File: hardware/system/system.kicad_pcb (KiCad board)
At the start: 2 copper layers, 226.6 x 87.2 mm, 45 parts, among them J1 CART_SOCKET_28P, J2 EXT_PINS, SW1 POWER, SW2 RESET, SW3 A, SW4 B, SW5 UP, SW6 DN, SW7 LF, SW8 RT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

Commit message: Bump system to 1.0-dev1
- Mirror charge symbol on back shell
- Remove button 3D models
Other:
- board text added: "V1.0-dev1"
- board text removed: "V1.0-dev0"

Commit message: Rewire screen regulator Vin to RAW
- Also add schematic PDFs
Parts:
- removed the BZ1 at (93.5, 140.2)
- removed the U3 at (63.3, 95.0)
- added REF**: Buzzer, system:BUZZER_CUTOUT, F.Cu at (93.5, 140.2)
- added REF**: SPI_DISPLAY, system:DIYMORE_2.42_IN_OLED_CUTOUT, F.Cu at (63.3, 95.0)
- D1, D2: value SB1100 -> SB120
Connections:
- C1 pad 1: VCC -> Net-(C1-Pad1)
- J1 pad 26: Net-(J1-Pad26) -> Net-(C1-Pad1)
- SW1 pad 3: Net-(J1-Pad26) -> Net-(C1-Pad1)
- U2 pad 2: VCC -> Net-(C1-Pad1)
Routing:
- net Net-(C1-Pad1): track 0.00 -> 150.4 mm
- net Net-(J1-Pad26): track 54.5 -> 0.00 mm
- net VCC: track 110.1 -> 78.5 mm
- net GND: vias 9 -> 10
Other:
- board text added: "V1.0-dev2"
- board text removed: "V1.0-dev1"

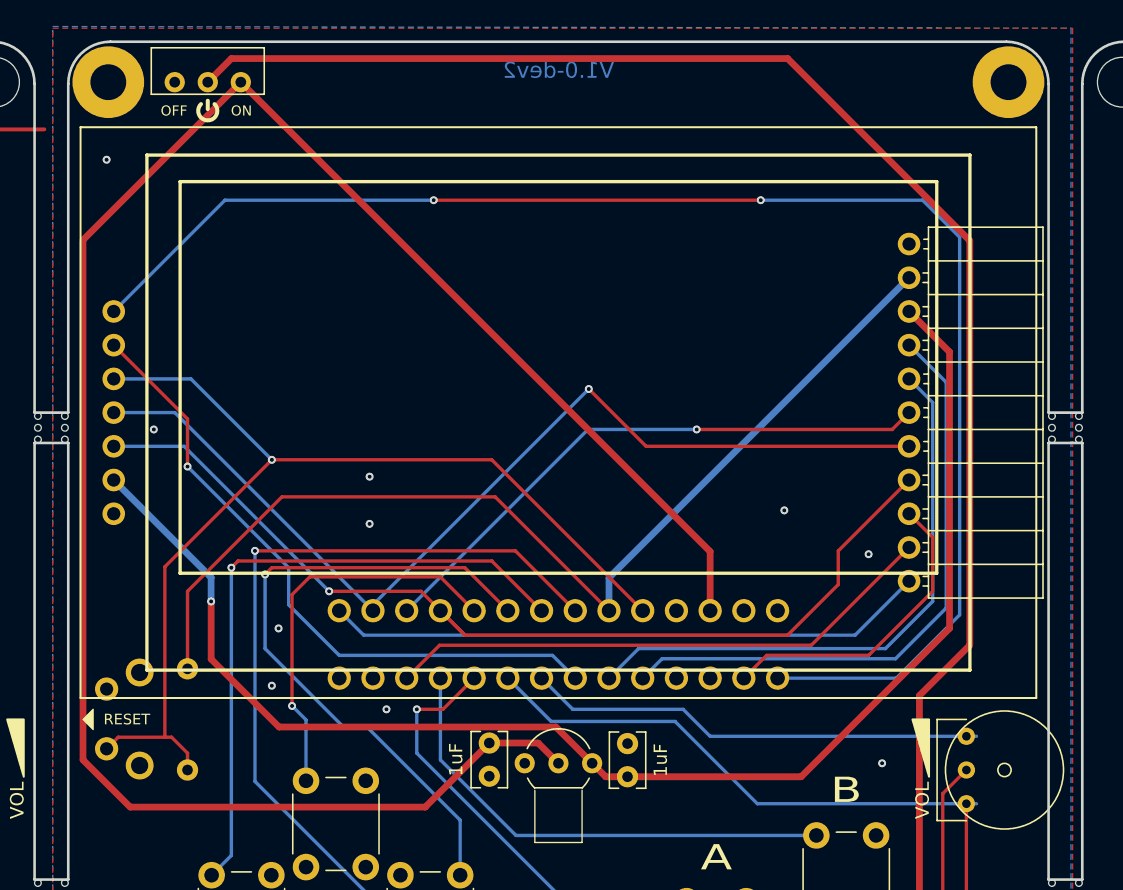
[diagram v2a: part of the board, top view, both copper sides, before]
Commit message: Connect power to VCC instead of RAW
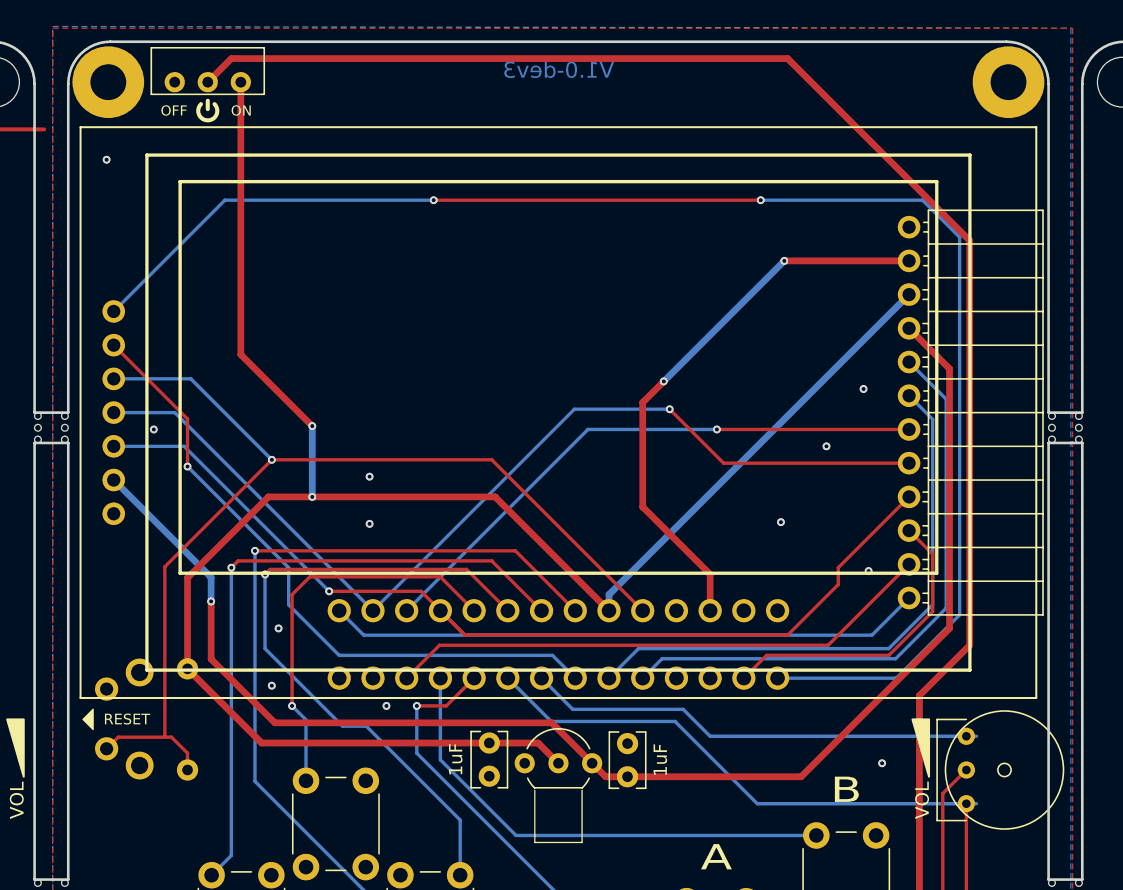
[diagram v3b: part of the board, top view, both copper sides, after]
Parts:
- removed the REF** at (93.5, 140.2)
- removed the REF** at (63.3, 95.0)
- removed the RV1 at (99.4, 121.9)
- added ?: SPI_DISPLAY, system:DIYMORE_2.42_IN_OLED_CUTOUT, F.Cu at (63.3, 95.0)
- added ?: Buzzer, system:BUZZER_CUTOUT, F.Cu at (93.5, 140.2)
- added ?: VOLUME 10K, system:VOLUME_LABEL, F.Cu at (99.4, 121.9)
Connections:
- C1 pad 1: Net-(C1-Pad1) -> VCC
- J1 pad 26: Net-(C1-Pad1) -> RAW
- J2 pad 10: D9_A9 -> D0
- J2 pad 11: D10_A10 -> D9_A9
- J2 pad 2: VCC -> RAW
- J2 pad 3: 3V3 -> VCC
- J2 pad 4: SDA -> 3V3
- J2 pad 5: SCL -> SDA
- J2 pad 6: MISO -> SCL
- J2 pad 7: MOSI -> MISO
- J2 pad 8: SCK -> MOSI
- J2 pad 9: D0 -> SCK
- SW1 pad 3: Net-(C1-Pad1) -> VCC
- U2 pad 2: Net-(C1-Pad1) -> VCC
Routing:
- net Net-(C1-Pad1): track 150.4 -> 0.00 mm
- net VCC: track 78.5 -> 142.2 mm, vias 0 -> 2
- net RAW: track 0.00 -> 42.3 mm, vias 0 -> 2
- net SDA: track 46.0 -> 44.7 mm
- net SCK: track 74.7 -> 73.5 mm
- net 3V3: track 105.6 -> 104.3 mm
- net SCL: track 44.3 -> 43.2 mm
- net MOSI: track 75.1 -> 74.1 mm
- net D9_A9: track 41.9 -> 41.4 mm
- net D10_A10: track 45.4 -> 44.8 mm
- net MISO: track 44.0 -> 43.5 mm
- net GND: vias 10 -> 12
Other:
- board text added: "V1.0-dev3"
- board text removed: "V1.0-dev2"

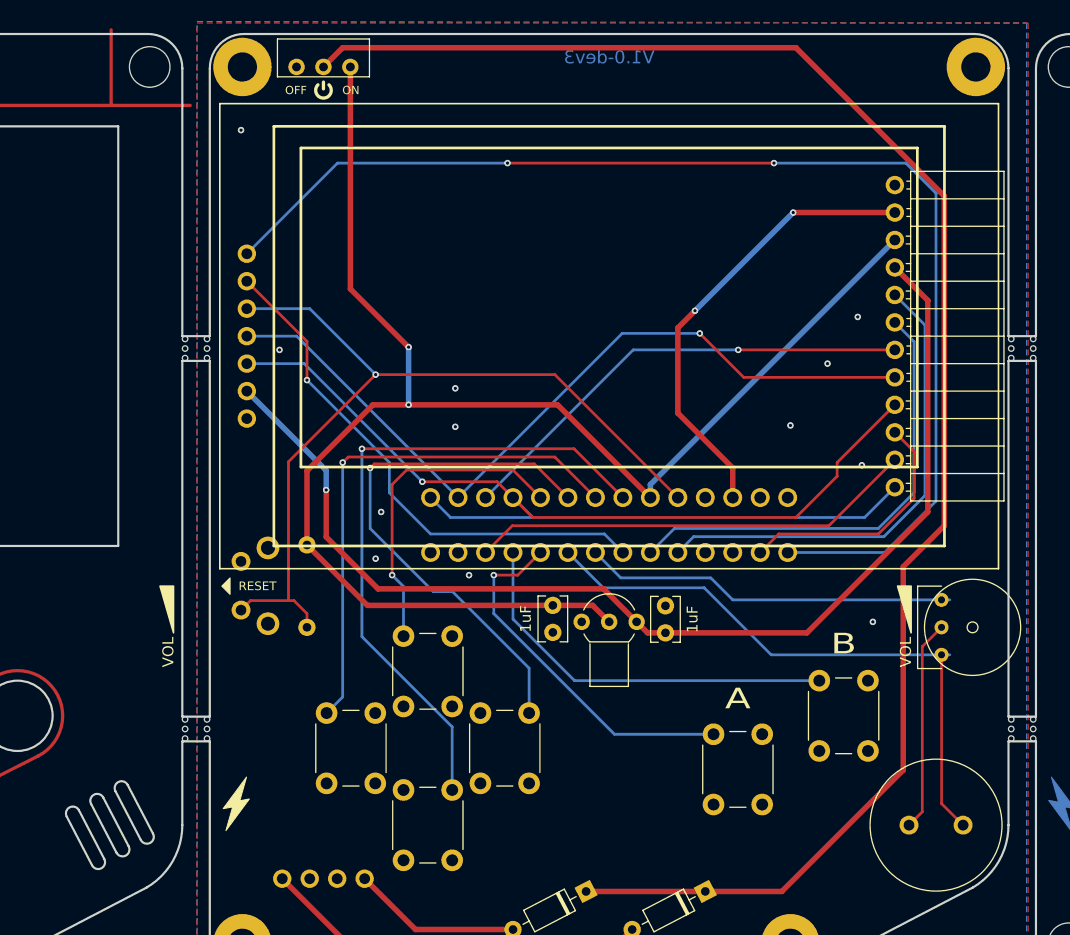
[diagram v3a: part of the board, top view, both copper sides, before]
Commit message: Connect display RES to D0/RX
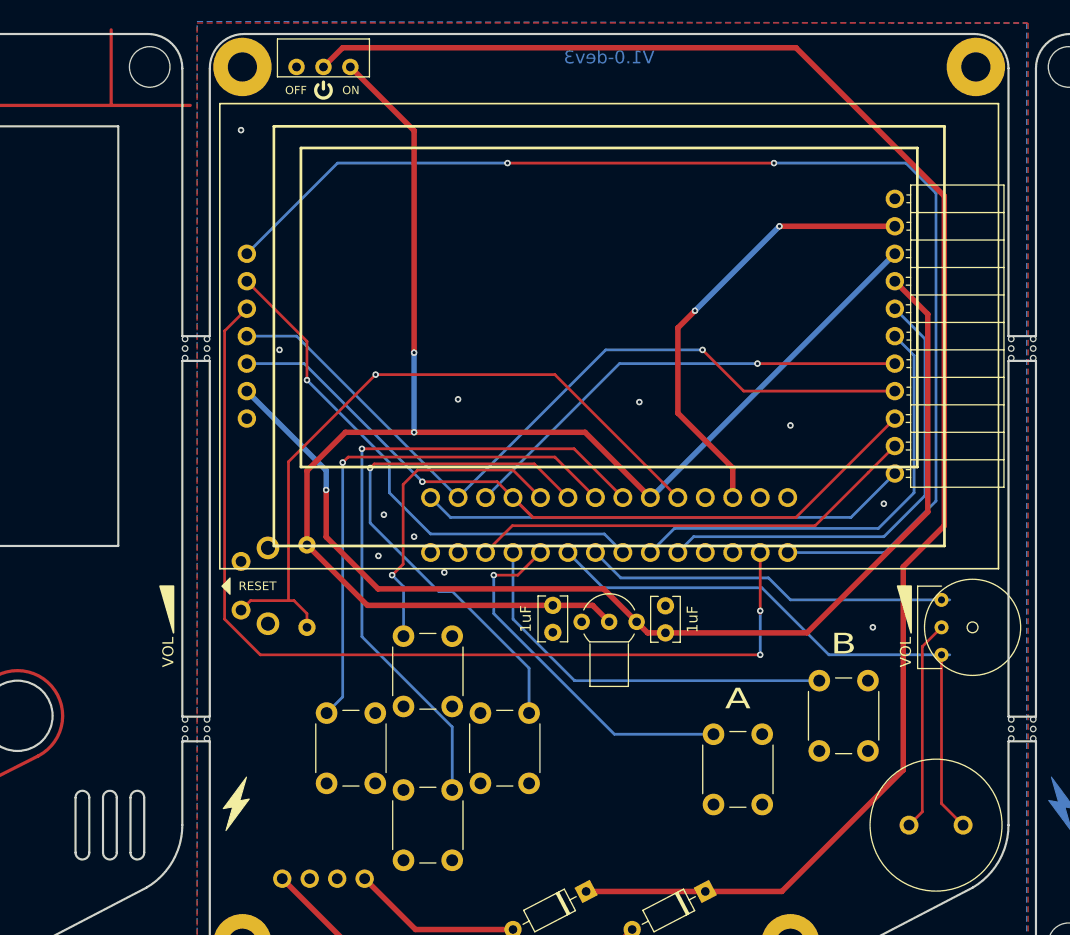
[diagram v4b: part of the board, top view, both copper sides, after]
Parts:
- removed ?: SPI_DISPLAY, system:DIYMORE_2.42_IN_OLED_CUTOUT
- removed ?: Buzzer, system:BUZZER_CUTOUT
- removed ?: VOLUME 10K, system:VOLUME_LABEL
- added **REF: Buzzer, system:BUZZER_CUTOUT, F.Cu at (93.5, 140.2)
- added **REF: Volume, system:VOLUME_LABEL, F.Cu at (99.4, 121.9)
- added REF**: DIYMORE_2.42_IN_OLED_CUTOUT, system:DIYMORE_2.42_IN_OLED_CUTOUT, F.Cu at (63.3, 95.0)
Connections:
- J1 pad 2: D0 -> Net-(J1-Pad2)
- J2 pad 10: D0 -> D9_A9
- J2 pad 11: D9_A9 -> D10_A10
- U3 pad 5: Net-(J1-Pad24) -> Net-(J1-Pad2)
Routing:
- net Net-(J1-Pad2): track 0.00 -> 89.9 mm, vias 0 -> 2
- net D0: track 23.1 -> 0.00 mm
- net Net-(J1-Pad24): track 79.5 -> 65.1 mm
- net SCL: track 43.2 -> 41.9 mm
- net 3V3: track 104.3 -> 103.1 mm
- net SDA: track 44.7 -> 43.5 mm
- net SCK: track 73.5 -> 72.2 mm
- net MOSI: track 74.1 -> 73.3 mm
- net Net-(J1-Pad19): track 29.8 -> 29.2 mm
- net VCC: track 142.2 -> 141.6 mm
- net MISO: track 43.5 -> 43.0 mm
- net D9_A9: track 41.4 -> 41.9 mm
- net D10_A10: track 44.8 -> 45.4 mm
- net RAW: track 42.3 -> 41.7 mm
- net GND: vias 12 -> 11

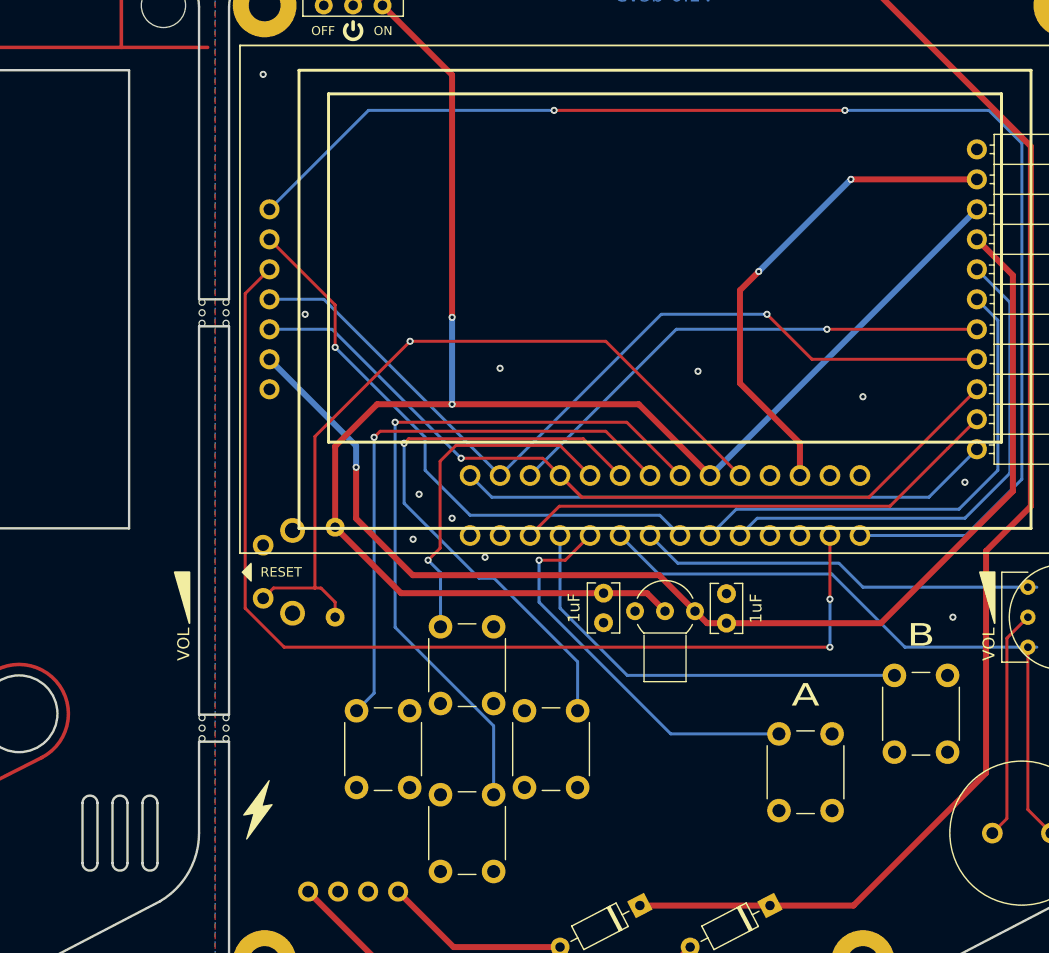
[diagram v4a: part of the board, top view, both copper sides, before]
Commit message: Update system PCB, fix speaker cutout
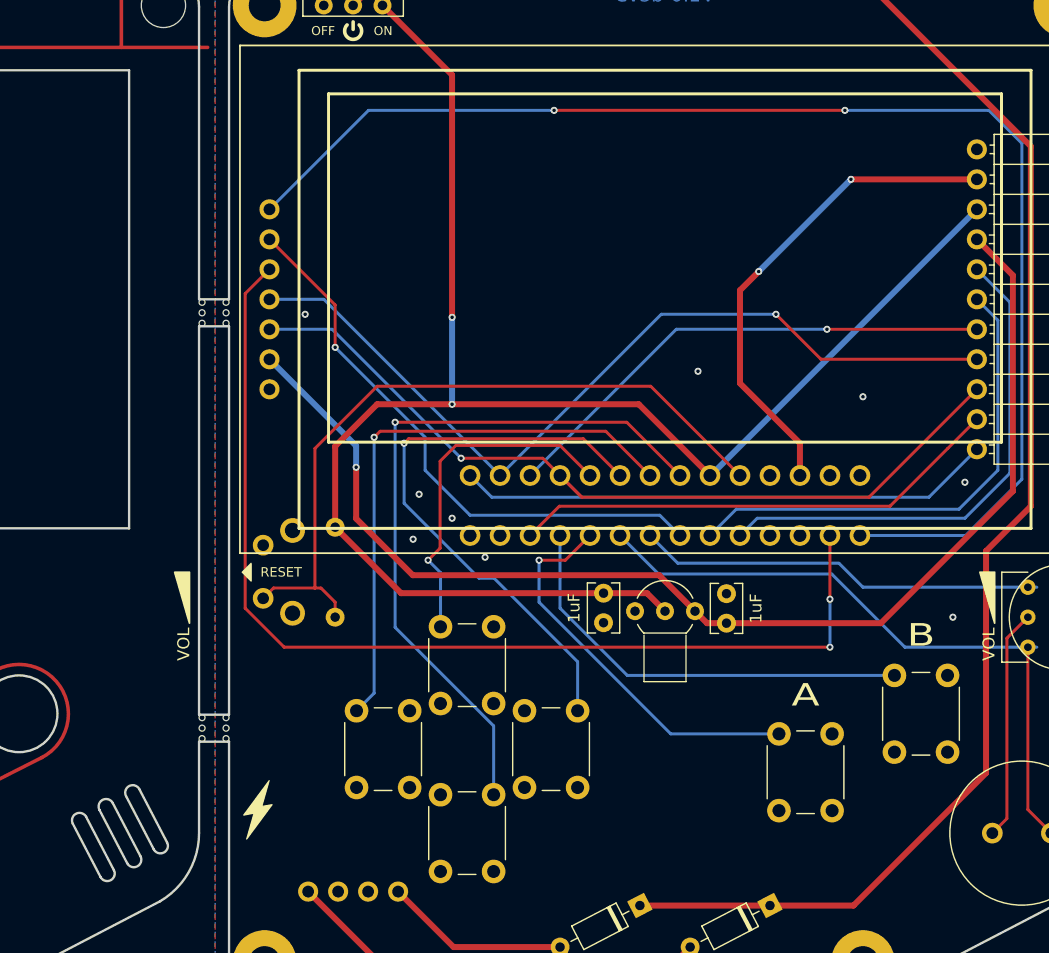
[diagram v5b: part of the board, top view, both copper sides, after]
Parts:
- turned **REF to 27.5 degrees
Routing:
- net Net-(J1-Pad24): track 65.1 -> 61.4 mm, vias 1 -> 0
- net GND: vias 11 -> 9

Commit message: Update EXT footprint
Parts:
- J2: value EXT_PINS -> EXTENSION PINS

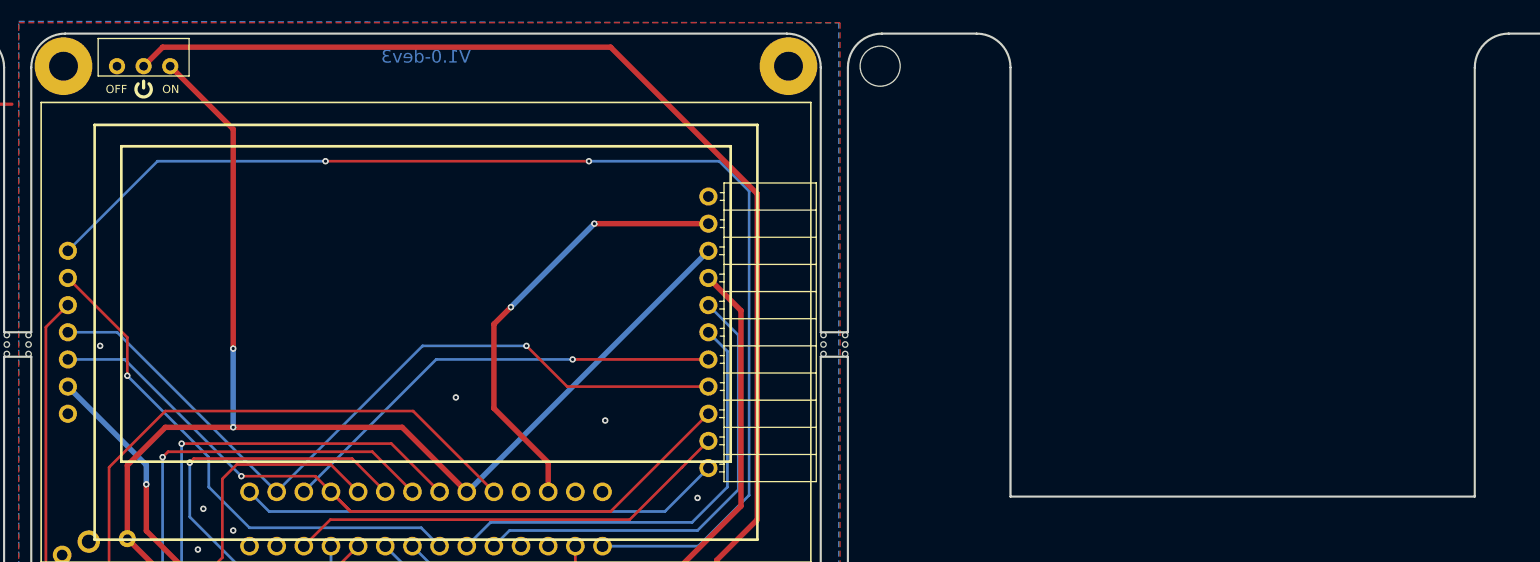
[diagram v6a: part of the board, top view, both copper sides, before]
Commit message: Update system board (start of 1.0dev4)
- Cover cart connector more
- Move EXT labels closer to edge
- Add cart grip cutout
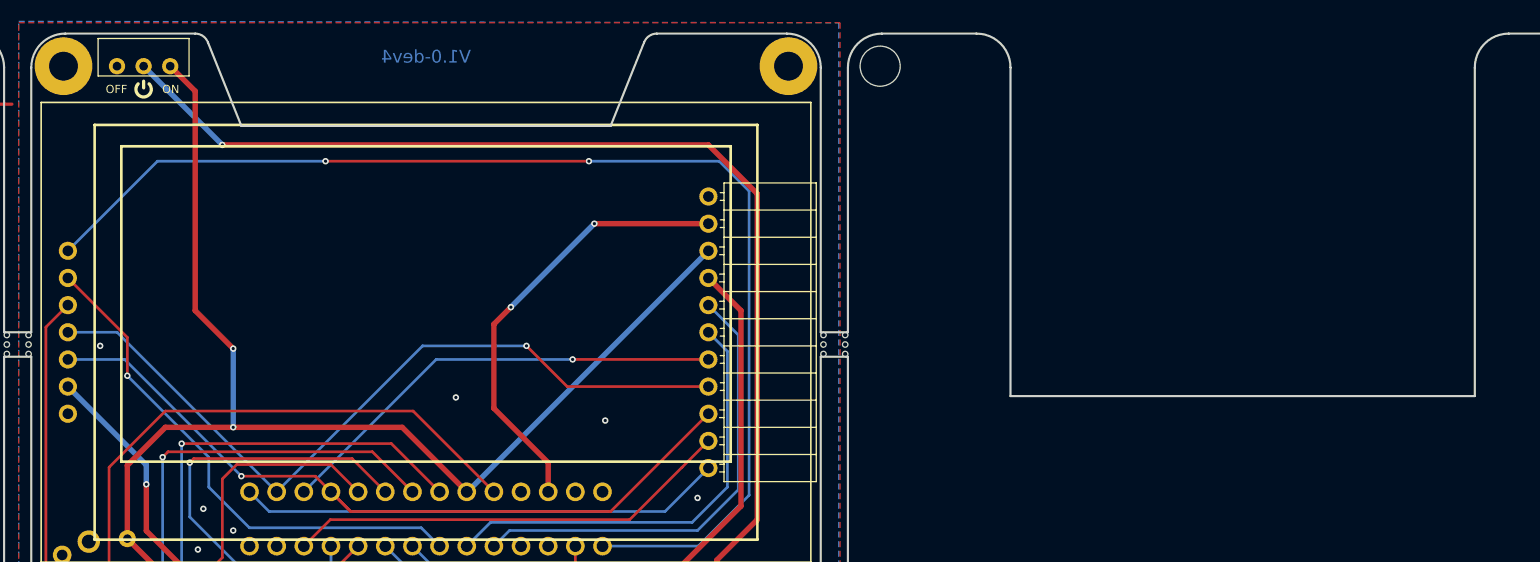
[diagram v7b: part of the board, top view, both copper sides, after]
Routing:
- net Net-(D1-Pad1): track 152.4 -> 151.0 mm, vias 0 -> 1
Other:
- outline, holes or cut-outs redrawn
- board text added: "V1.0-dev4"
- board text removed: "V1.0-dev3"
